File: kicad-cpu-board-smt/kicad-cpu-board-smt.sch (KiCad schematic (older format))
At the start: 56 parts, among them J1 ICSP Header, J2 Conn_01x10_Male, J3 Conn_01x16_Female, J4 Conn_02x05_Odd_Even, Q1 2N7002, Q2 2N7002, Q3 2N7002, Q4 2N7002, U1 AMS1117-5.0, U2 AMS1117-3.3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

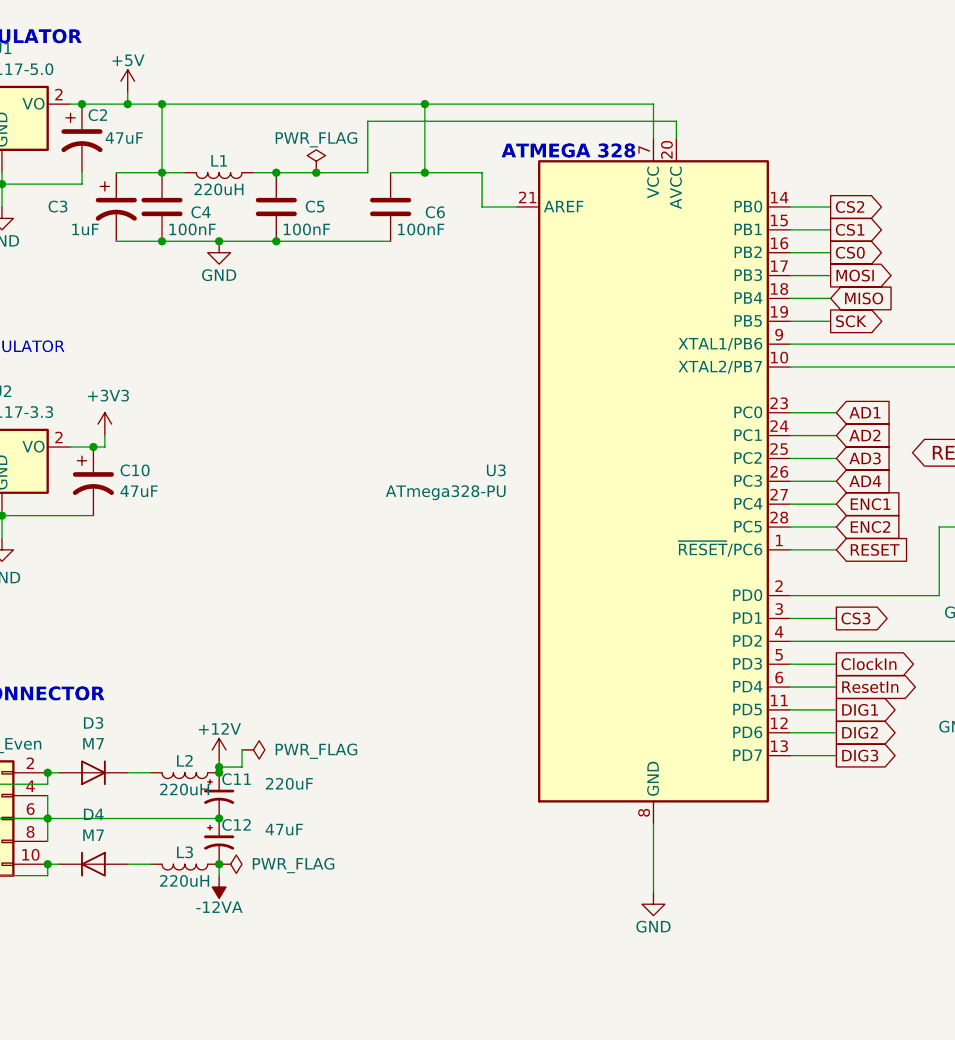
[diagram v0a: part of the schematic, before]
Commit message: Fixing CPU footprint on SMT board and updating bom + gerbers
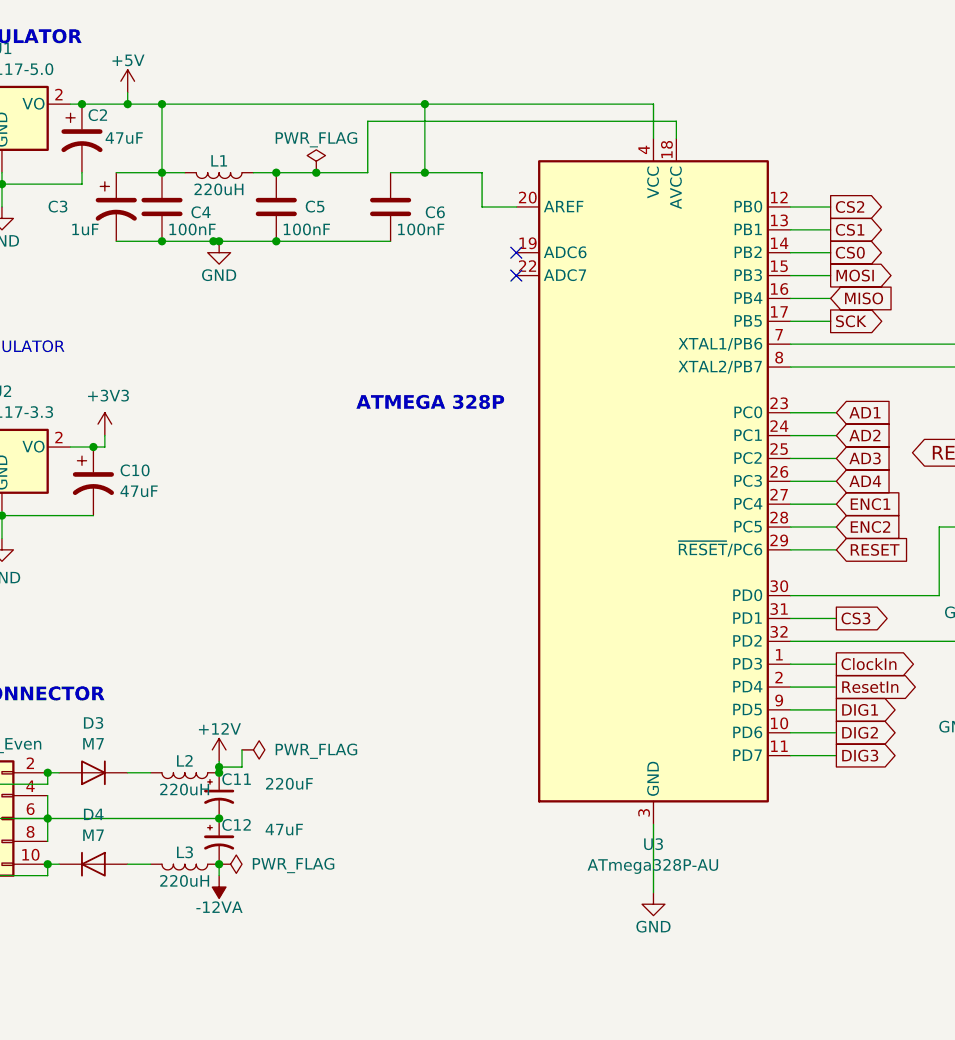
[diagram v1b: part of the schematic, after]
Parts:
- removed U3: ATmega328-PU, Housings_QFP:LQFP-32_7x7mm_Pitch0.8mm, symbol MCU_Microchip_ATmega:ATmega328P-PU
- added U3: ATmega328P-AU, Housings_QFP:TQFP-32_7x7mm_Pitch0.8mm, symbol MCU_Microchip_ATmega:ATmega328-AU
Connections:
- net +5V: now also U3.20 (AREF), U3.4 (VCC), U3.6 (VCC)
- net AD1: now also U3.23 (PC0)
- net AD2: now also U3.24 (PC1)
- net AD3: now also U3.25 (PC2)
- net AD4: now also U3.26 (PC3)
- net CS0: now also U3.14 (PB2)
- net CS1: now also U3.13 (PB1)
- net CS2: now also U3.12 (PB0)
- net CS3: now also U3.31 (PD1)
- net ClockIn: now also U3.1 (PD3)
- net DIG1: now also U3.9 (PD5)
- net DIG2: now also U3.10 (PD6)
- net DIG3: now also U3.11 (PD7)
- net ENC1: now also U3.27 (PC4)
- net ENC2: now also U3.28 (PC5)
- net GND: now also U3.21 (GND), U3.3 (GND), U3.5 (GND)
- net MISO: now also U3.16 (PB4)
- net MOSI: now also U3.15 (PB3)
- net RESET: now also U3.29 (~RESET~/PC6)
- net ResetIn: now also U3.2 (PD4)
- net SCK: now also U3.17 (PB5)
- net at C7.2, R1.2, Y1.1: now also U3.7 (XTAL1/PB6)
- net at C8.2, R1.1, Y1.3: now also U3.8 (XTAL2/PB7)
- net at D1.1 (K), R3.2: now also U3.30 (PD0)
- net at D2.1 (K), R4.2: now also U3.32 (PD2)
- net at C5.1, L1.1: now also U3.18 (AVCC)
- no-connect marks 0 -> 2
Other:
- note added: "ATMEGA 328P"
- note removed: "ATMEGA 328"
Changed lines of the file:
@@
 Text Notes 2025 850  2    60   ~ 12
 5V REGULATOR
-Text Notes 4450 1350 2    60   ~ 12
-ATMEGA 328
+Text Notes 3875 2450 2    60   ~ 12
+ATMEGA 328P
 Text Notes 9400 6400 2    60   ~ 12
 FLASH MEMORY
@@
 Connection ~ 2625 1700
 Wire Wire Line
-	2375 1700 2625 1700
+	2375 1700 2600 1700
 Connection ~ 2875 1400
 Wire Wire Line
@@
 $EndComp
 $Comp
-L MCU_Microchip_ATmega:ATmega328P-PU U3
-U 1 1 5DD69A10
-P 4525 2750
-F 0 "U3" H 3884 2796 50  0000 R CNN
-F 1 "ATmega328-PU" H 3884 2705 50  0000 R CNN
-F 2 "Housings_QFP:LQFP-32_7x7mm_Pitch0.8mm" H 4525 2750 50  0001 C CIN
-F 3 "http://ww1.microchip.com/downloads/en/DeviceDoc/ATmega328_P%20AVR%20MCU%20with%20picoPower%20Technology%20Data%20Sheet%2040001984A.pdf" H 4525 2750 50  0001 C CNN
-F 4 "C14877" H 4525 2750 50  0001 C CNN "LCSC Part Number"
-F 5 "ATMEGA328P-AU" H 4525 2750 50  0001 C CNN "MFG Part Number"
-F 6 "Microchip" H 4525 2750 50  0001 C CNN "Manufacturer"
-	1    4525 2750
-	1    0    0    -1
-$EndComp
-$Comp
 L Connector:Conn_01x10_Male J2
 U 1 1 5DCFEE3D
@@
 Wire Wire Line
 	6500 2250 6750 2250
+$Comp
+L MCU_Microchip_ATmega:ATmega328-AU U3
+U 1 1 5E1AB25F
+P 4525 2750
+F 0 "U3" H 4525 1161 50  0000 C CNN
+F 1 "ATmega328P-AU" H 4525 1070 50  0000 C CNN
+F 2 "Housings_QFP:TQFP-32_7x7mm_Pitch0.8mm" H 4525 2750 50  0001 C CIN
+F 3 "http://ww1.microchip.com/downloads/en/DeviceDoc/ATmega328_P%20AVR%20MCU%20with%20picoPower%20Technology%20Data%20Sheet%2040001984A.pdf" H 4525 2750 50  0001 C CNN
+	1    4525 2750
+	1    0    0    -1
+$EndComp
+NoConn ~ 3925 1750
+NoConn ~ 3925 1850
+Connection ~ 2600 1700
+Wire Wire Line
+	2600 1700 2625 1700
 $EndSCHEMATC

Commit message: Tweaking tracerouting
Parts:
- C1, C13, C14, C4, C5, C6, C9: Digikey Part Number (none) -> 399-1100-6-ND; MFG Part Number CC0603KRX7R9BB104 -> C0603C104Z3VACTU; Manufacturer YAGEO -> Kemet
- C10, C12, C2: Digikey Part Number (none) -> 493-2225-6-ND; MFG Part Number VES470M1HTR-0607 -> UWT1H470MCL1GS; Manufacturer LELON -> Nichicon
- C11: Digikey Part Number (none) -> 493-2179-6-ND; MFG Part Number VZH221M1VTR-1010K -> UWT1C221MCL1GS; Manufacturer LELON -> Nichicon
- C15, C16, C7, C8: Digikey Part Number (none) -> 399-7874-6-ND; MFG Part Number CL10C220JB8NNNC -> C0603C220J1GACTU; Manufacturer SAMSUNG -> Kemet
- C3: Digikey Part Number (none) -> 493-9985-6-ND; LCSC Part Number C108053 -> 493-9985-6-ND; MFG Part Number VES470M1HTR-0607 -> UUX2G010MNL1GS; Manufacturer LELON -> Nichicon
- D1, D2: value 1SMA4733A -> 1SMB5918BT3G; footprint Diodes_SMD:D_SMA_Handsoldering -> Diodes_SMD:D_SMA-SMB_Universal_Handsoldering; Digikey Part Number (none) -> 1SMB5918BT3GOSDKR-ND; MFG Part Number 1SMA4733A -> 1SMB5918BT3G; Manufacturer MDD -> ON Semiconductor
- D3, D4: value M7 -> S1KB; footprint Diodes_SMD:D_SMA_Handsoldering -> Diodes_SMD:D_SMA-SMB_Universal_Handsoldering; Digikey Part Number (none) -> S1KB-FDIDKR-ND; LCSC Part Number C95872 -> S1KB-FDIDKR-ND; MFG Part Number M7 -> S1KB-13-F; Manufacturer MDD -> Diodes Incorporated
- J1: Digikey Part Number (none) -> 609-3218-ND; MFG Part Number (none) -> 67996-406HLF; Manufacturer (none) -> Amphenol
- J2: Digikey Part Number (none) -> 609-3285-ND; MFG Part Number (none) -> 68001-410HLF; Manufacturer (none) -> Amphenol
- J3: value Conn_01x16_Female -> Conn_01x16_Male; Digikey Part Number (none) -> 609-3267-ND; MFG Part Number (none) -> 68000-416HLF; Manufacturer (none) -> Amphenol
- J4: Digikey Part Number (none) -> 609-3243-ND; MFG Part Number (none) -> 67997-410HLF; Manufacturer (none) -> Amphenol
- L1, L2, L3: Digikey Part Number (none) -> 445-1545-6-ND; MFG Part Number NLV32T-221J-PF -> NLCV32T-221K-PF
- Q1, Q2, Q3, Q4: Digikey Part Number (none) -> 2N7002LT1GOSDKR-ND; LCSC Part Number C8545 -> (none); MFG Part Number 2N7002 -> 2N7002LT1G; Manufacturer CJ -> ON Semiconductor
- R1: Digikey Part Number (none) -> RMCF0603FT1M00DKR-ND; MFG Part Number 0603WAF1004T5E -> RMCF0603FT1M00; Manufacturer Uniroyal -> Stackpole Electronics, Inc
- R10, R11, R12, R5, R6, R7, R8, R9: value 1K -> 1k; Digikey Part Number (none) -> RMCF0603FT1K00DKR-ND; LCSC Part Number C21190 -> (none); MFG Part Number 0603WAF1001T5E -> RMCF0603FT1K00; Manufacturer Uniroyal -> Stackpole Electronics, Inc
- R13, R16, R3, R4: Digikey Part Number (none) -> RMCF0603FT1K00DKR-ND; LCSC Part Number C21190 -> (none); MFG Part Number 0603WAF1001T5E -> RMCF0603FT1K00; Manufacturer Uniroyal -> Stackpole Electronics, Inc
- R14, R15, R17, R18, R2: Digikey Part Number (none) -> RMCF0603FT10K0DKR-ND; MFG Part Number 0603WAF1002T5E -> RMCF0603FT10K0; Manufacturer Uniroyal -> Stackpole Electronics, Inc
- U1: Digikey Part Number (none) -> NCP1117ST50T3GOSDKR-ND; MFG Part Number AMS1117-5.0 -> NCP1117ST50T3G; Manufacturer AMS -> ON Semiconductor
- U2: Digikey Part Number (none) -> NCP1117ST33T3GOSDKR-ND; MFG Part Number AMS1117-3.3 -> NCP1117ST33T3G; Manufacturer AMS -> ON Semiconductor
- U3: Digikey Part Number (none) -> ATMEGA328P-AURDKR-ND; MFG Part Number (none) -> ATMEGA328P-AUR; Manufacturer (none) -> Microchip Technology
- U4: Digikey Part Number (none) -> W25Q80DVSNIG-ND; MFG Part Number W25Q80DVSNIG TR -> W25Q80DVSNIG
- U5: Digikey Part Number (none) -> 296-1282-6-ND; MFG Part Number TL072CDT -> TL072CDR; Manufacturer ST -> Texas Instruments
- U6: Digikey Part Number (none) -> MCP4822-E/SN-ND
- Y1: Digikey Part Number (none) -> SER4069DKR-ND; MFG Part Number (none) -> TSX-3225 16.0000MF09Z-AC0; Manufacturer (none) -> Epson
